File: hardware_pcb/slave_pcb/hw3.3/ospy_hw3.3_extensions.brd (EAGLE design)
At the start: 128.6 x 109 mm, 56 parts, among them IC1 74HC595D, K1 4052, K2 4052, K3 4052, K4 4052, K5 4052, K6 4052, K7 4052, K8 4052

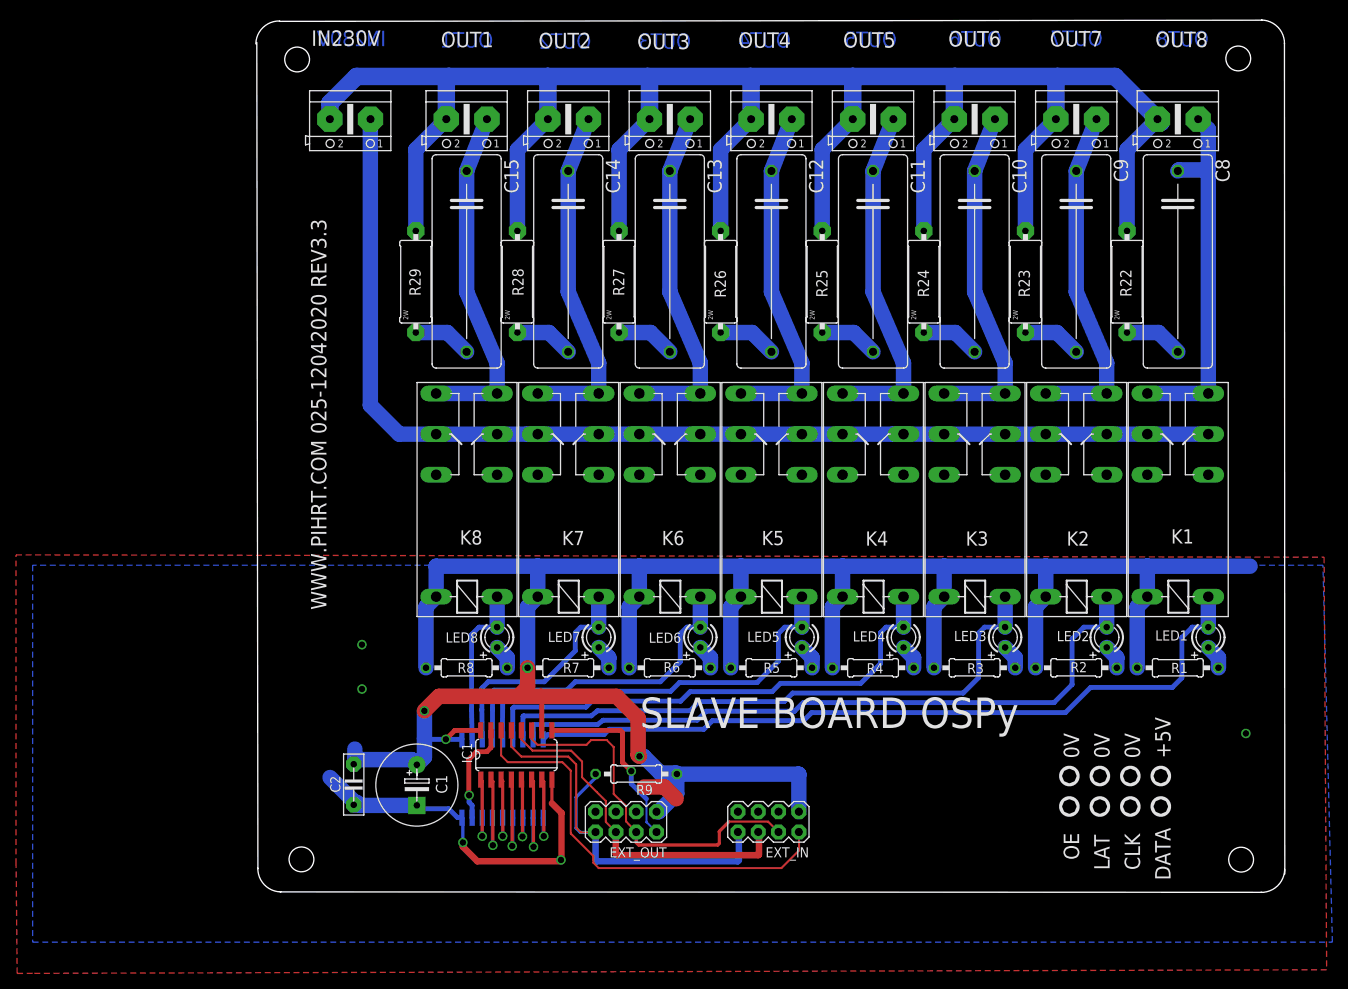
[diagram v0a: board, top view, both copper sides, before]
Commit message: fixed data for slave board HW3.3 (board outline)
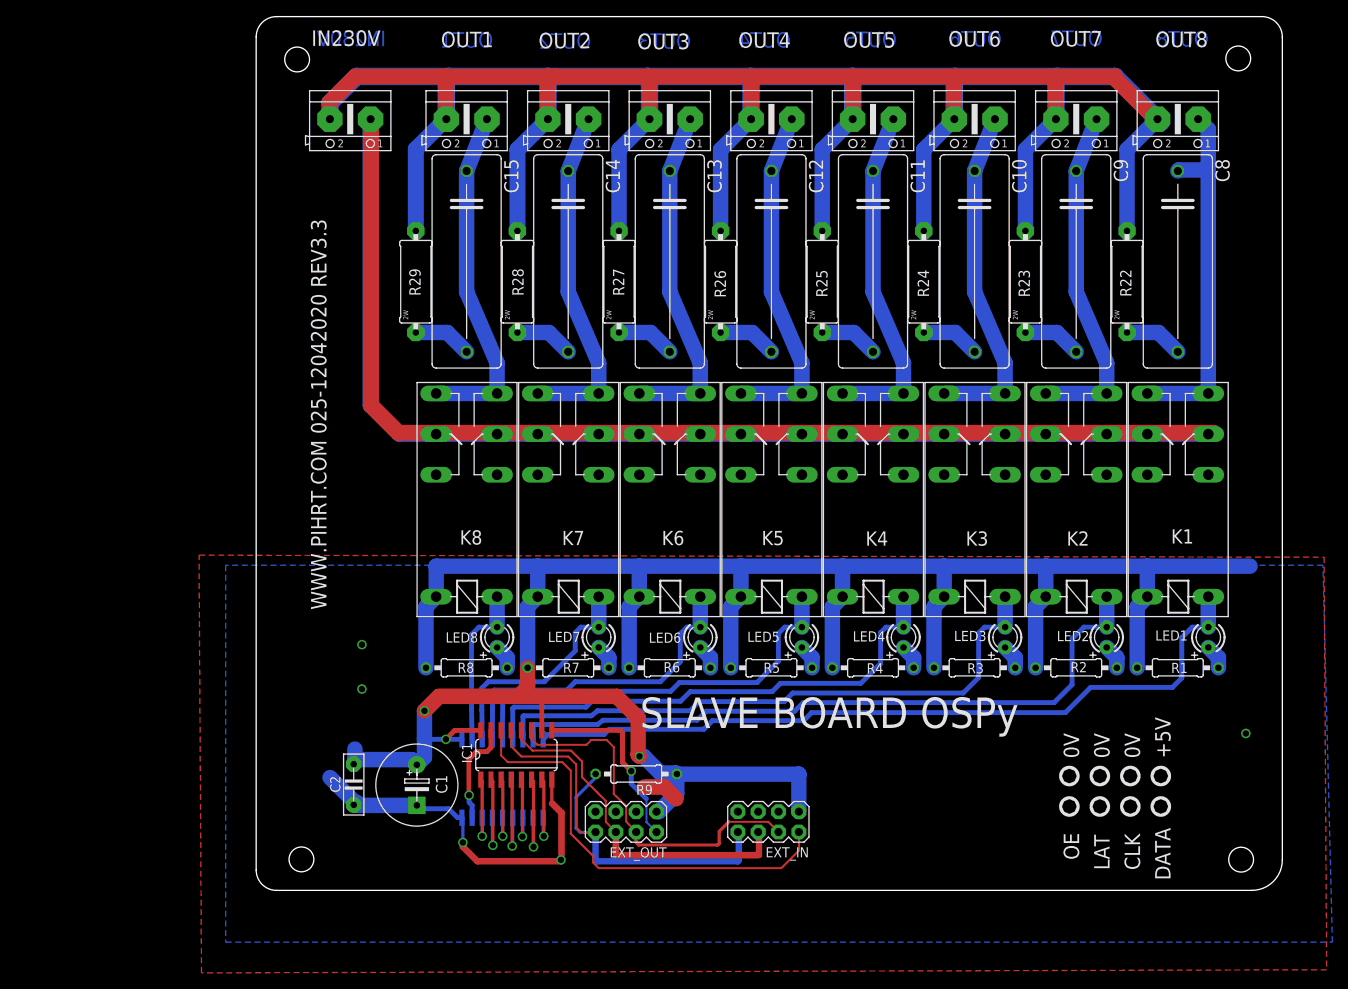
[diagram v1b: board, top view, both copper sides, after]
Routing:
- net NEUTRAL_230V: track 272.8 -> 420.7 mm
- net N$1: track 0.00 -> 142.4 mm
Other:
- board size 128.6 x 109 mm -> 128.3 x 109.2 mm
